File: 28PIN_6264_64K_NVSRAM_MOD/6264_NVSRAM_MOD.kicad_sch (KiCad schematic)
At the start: 18 parts, among them J1 Conn_01x02, U1 TL431DBZ, U10 TC5564APL_Adapter, U2 74AHC2G00, U3 STK12C68

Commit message: Updated silkscreen w. new naming scheme.
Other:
- company: (none) -> Copyright Dr. Matthew Swabey
- title: (none) -> 6264_NVSRAM_MOD
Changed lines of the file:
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@@
 (kicad_sch (version 20211123) (generator eeschema)
   (paper "USLetter")
+  (title_block
+    (title "6264_NVSRAM_MOD")
+    (date "2022-11-12")
+    (rev "V1")
+    (company "Copyright Dr. Matthew Swabey")
+  )
   (junction (at 90.17 74.93) (diameter 0) (color 0 0 0 0)
   )

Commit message: Updated title block on schematics. Minor silkscreen tweak to 24PIN 6116
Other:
- company: Copyright Dr. Matthew Swabey -> (none)
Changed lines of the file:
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@@
     (date "2022-11-12")
     (rev "V1")
-    (company "Copyright Dr. Matthew Swabey")
+    (comment 1 "Copyright Dr. Matthew Swabey")
   )
   (junction (at 90.17 74.93) (diameter 0) (color 0 0 0 0)

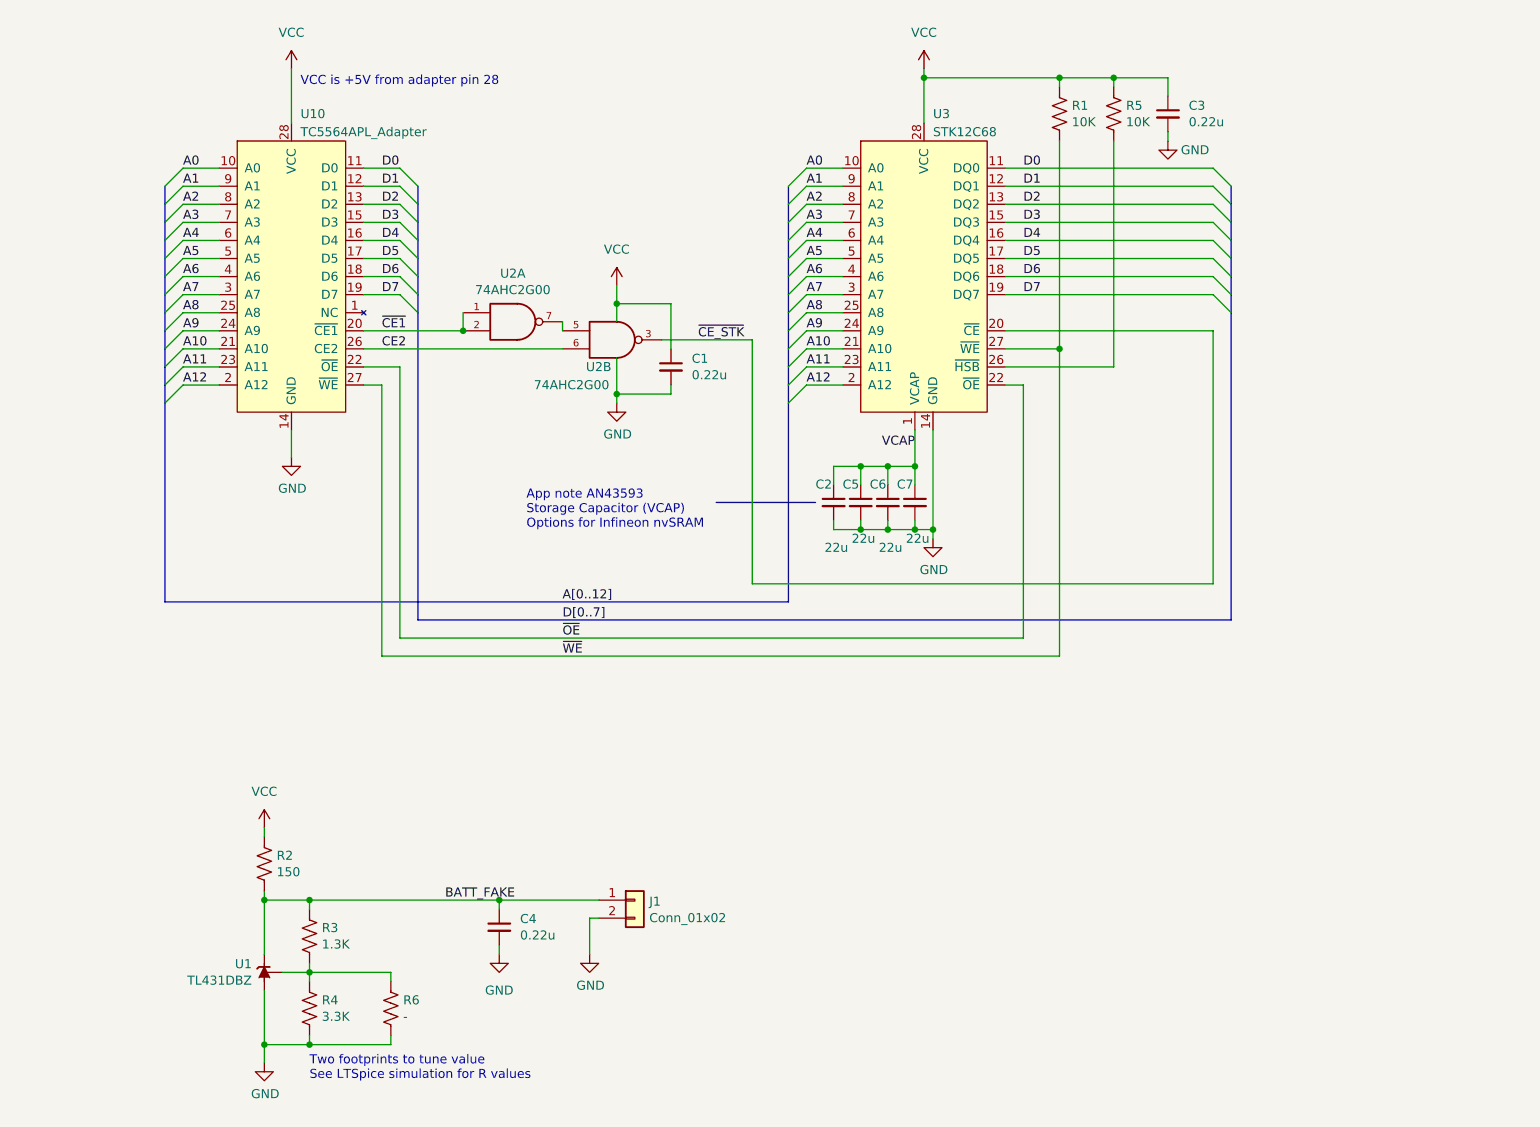
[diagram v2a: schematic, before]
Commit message: Updated to KiCAD 7 and library updates.
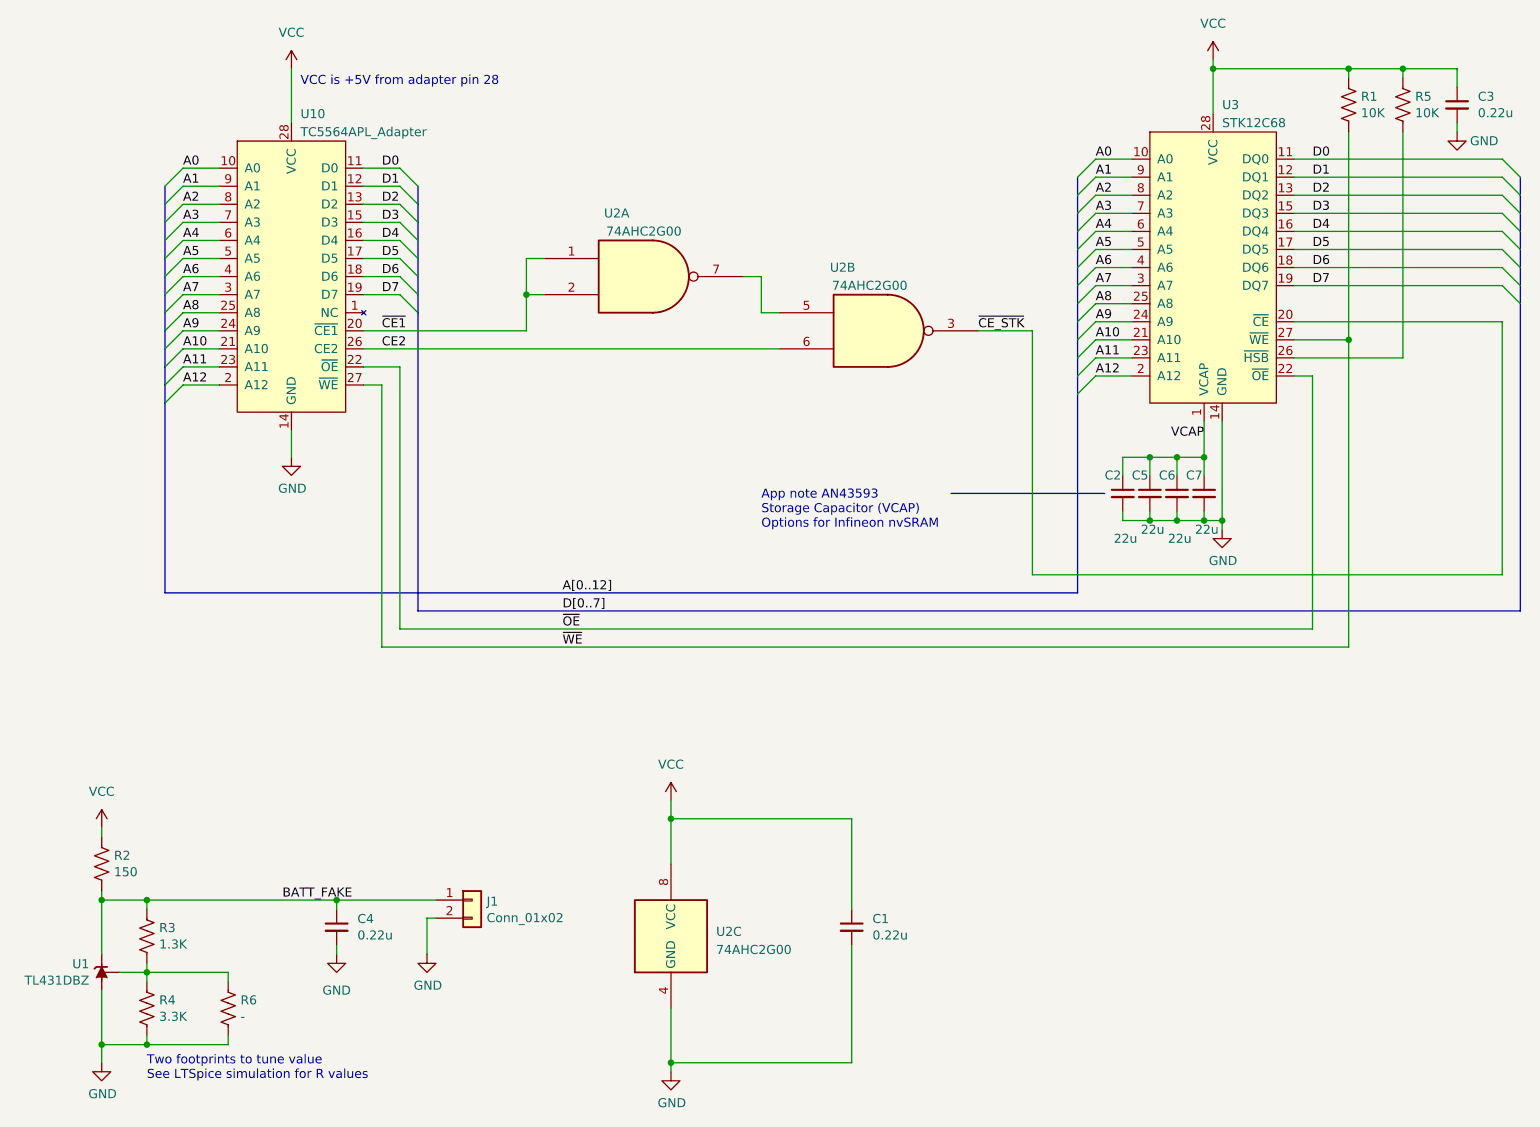
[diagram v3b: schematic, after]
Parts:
- added unit 3 of U2
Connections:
- net GND: now also U2.4 (GND); no longer U2.4 (GND), U2.4 (GND)
- net VCC: now also U2.8 (VCC); no longer U2.8 (VCC), U2.8 (VCC)
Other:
- moved on the sheet: C1, C2, C3, C4, C5, C6, C7, J1, R1, R2, R3, R4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
